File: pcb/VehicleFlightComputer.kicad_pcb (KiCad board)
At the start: 4 copper layers, 50 x 50 mm, 65 parts, among them J1 FFC2B28-24-G, J3 USB_C_Receptacle, J4 Debug, Q1 S8050, SW1 B3U-1000P, SW2 B3U-1000P, U1 STM32H533VET6, U2 LIS2MDL, U3 LSM6DSV32X, U4 MCP2221A-I/ST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

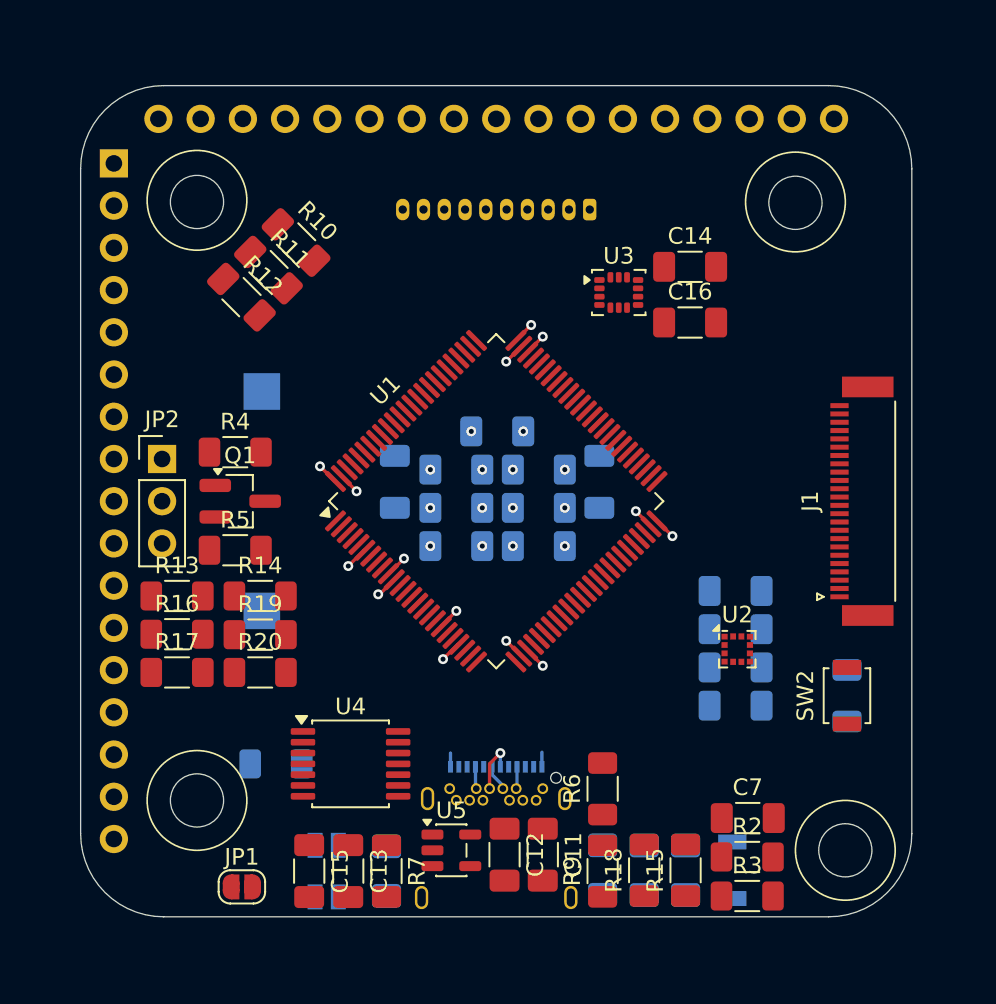
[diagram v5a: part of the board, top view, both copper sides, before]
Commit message: Updated vehicle stack-up edge-cuts for `VehicleMiscellaneousBoard` and `VehicleFlightComputer`.
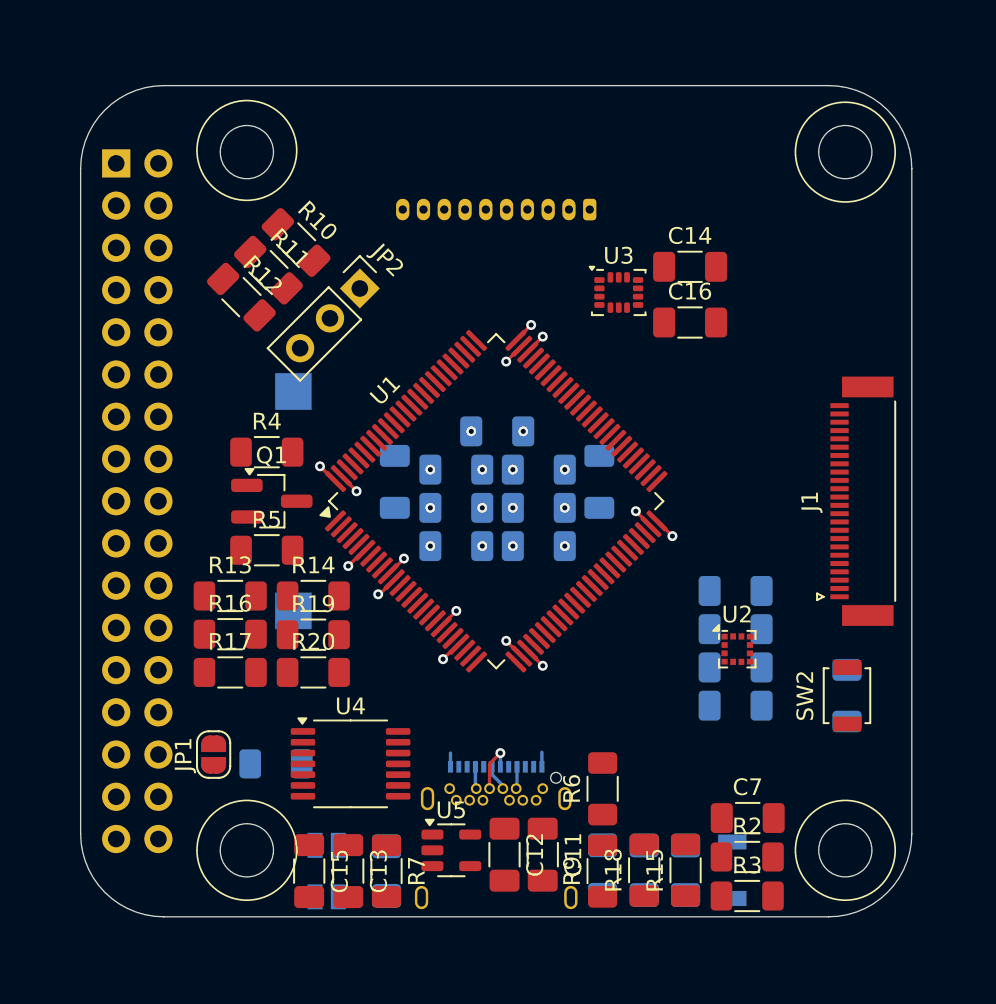
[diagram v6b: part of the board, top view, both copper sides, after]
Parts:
- removed H1, H3: MountingHole, MountingHole:MountingHole_3.2mm_M3
- moved JP2 15.7 mm to (141.8, 87.2), turned to -45 degrees
- moved JP1 8.14 mm to (133.0, 115.2), turned to 90 degrees
- moved H2 4.24 mm to (135.0, 79.0)
- moved H4 4.24 mm to (135.0, 121.0)
- moved R13 3.20 mm to (134.0, 105.7)
- moved R14 3.20 mm to (139.0, 105.7)
- moved R16 3.20 mm to (134.0, 108.0)
- moved R17 3.20 mm to (134.0, 110.3)
- moved R19 3.20 mm to (139.0, 108.0)
- moved R20 3.20 mm to (139.0, 110.3)
- moved BZ1 1.90 mm to (137.8, 100.0)
- moved Q1 1.90 mm to (136.5, 100.0)
- moved R4 1.90 mm to (136.2, 97.0)
- moved R5 1.90 mm to (136.2, 103.0)

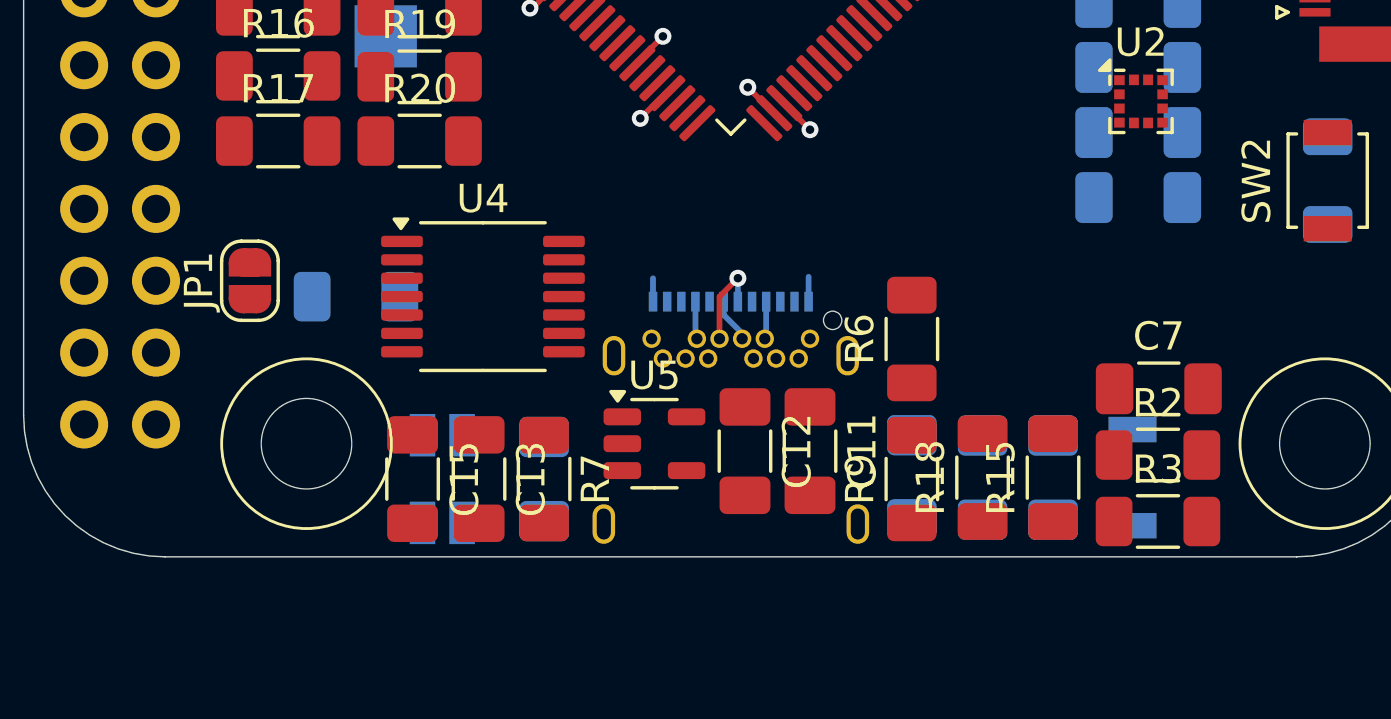
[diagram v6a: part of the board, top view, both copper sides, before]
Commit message: Placed footprints and routed USB-UART bridge and reset mechanism for `VehicleFlightComputer`.
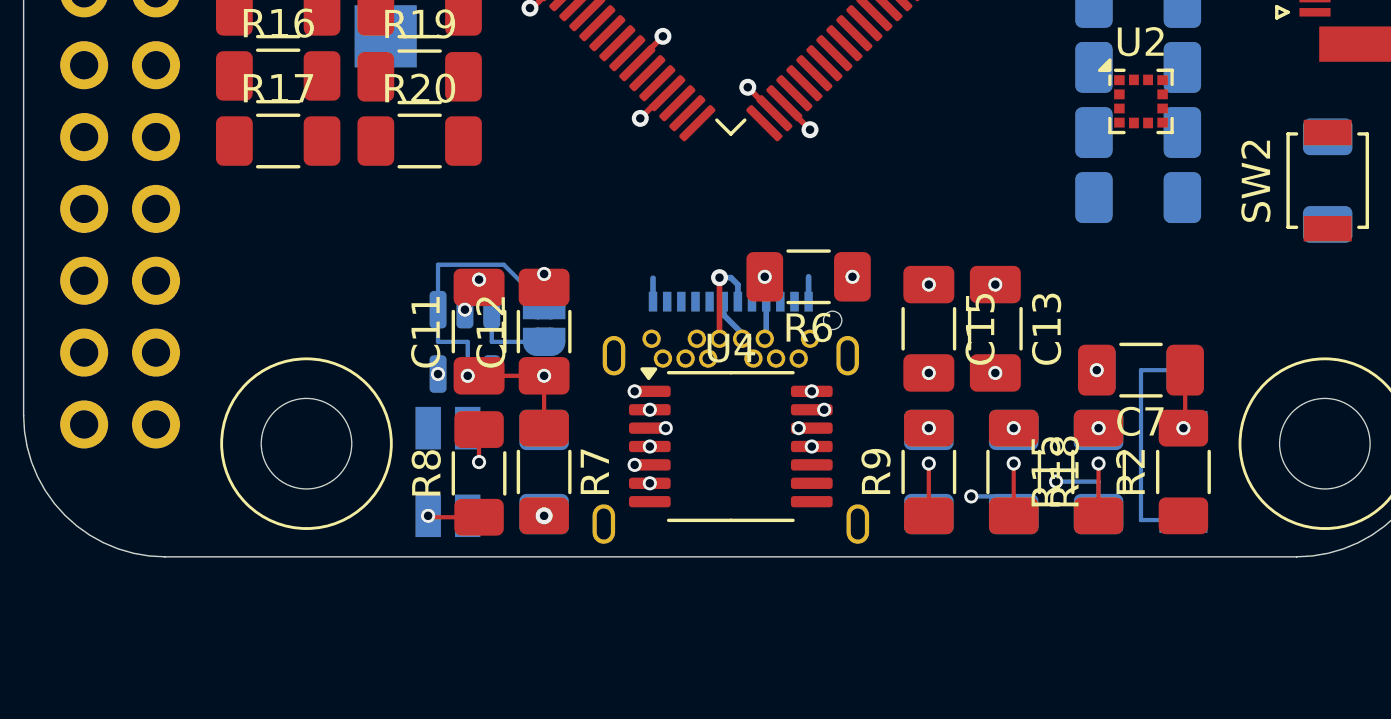
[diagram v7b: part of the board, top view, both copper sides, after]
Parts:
- JP1, R3, U5: moved to B.Cu
- R8: moved to F.Cu
- moved C13 19.0 mm to (159.3, 116.9)
- moved C15 19.0 mm to (157.0, 116.9)
- moved C11 12.4 mm to (141.1, 117.0), turned to 90 degrees
- moved JP1 10.5 mm to (143.4, 116.7), turned to -90 degrees
- moved U4 10.2 mm to (150.0, 121.1)
- moved C12 8.26 mm to (143.4, 117.0), turned to 90 degrees
- moved R8 7.61 mm to (141.1, 122.1), turned to 90 degrees
- moved U5 7.61 mm to (140.6, 117.4), turned to -90 degrees
- moved R3 5.38 mm to (164.5, 118.4), turned to 180 degrees
- moved R6 4.26 mm to (152.8, 115.1), turned to 180 degrees
- moved SW1 1.81 mm to (166.0, 122.0), turned to -90 degrees
- moved D3 1.62 mm to (163.0, 122.0)
- moved R15 1.62 mm to (163.0, 122.0)
- moved D4 1.12 mm to (160.0, 122.0)
- moved R18 1.12 mm to (160.0, 122.0), turned to -90 degrees
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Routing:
- net Net-(JP1-A): track 2.66 -> 24.6 mm, vias 0 -> 2
- net Net-(D3-K): track 0.00 -> 19.6 mm, vias 0 -> 2
- net serial_reset: track 0.00 -> 18.1 mm, vias 0 -> 2
- net Net-(D4-K): track 0.00 -> 15.3 mm, vias 0 -> 2
- net serial_rx: track 0.00 -> 13.8 mm, vias 0 -> 1
- net serial_tx: track 0.00 -> 11.6 mm, vias 0 -> 1
- net RESET: track 0.00 -> 8.73 mm, vias 0 -> 1
- net Net-(R3-Pad1): track 0.00 -> 8.35 mm
- net +3.3V: track 10.6 -> 18.0 mm, vias 15 -> 24
- net Net-(U4-D-): track 3.24 -> 9.36 mm, vias 1 -> 2
- net Net-(U4-D+): track 1.58 -> 7.27 mm, vias 0 -> 1
- net Net-(JP1-B): track 0.00 -> 2.99 mm
- net Net-(J3-CC1): track 0.00 -> 1.07 mm, vias 0 -> 1
- net Net-(D4-A): vias 0 -> 1
- net Net-(D3-A): vias 0 -> 1
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
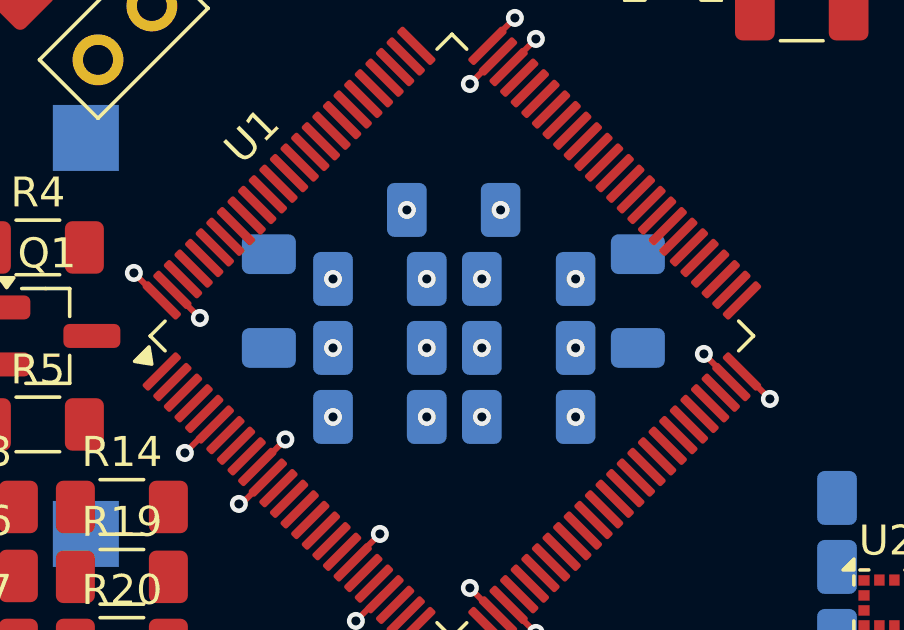
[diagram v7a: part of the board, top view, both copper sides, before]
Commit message: Routed VCAP.
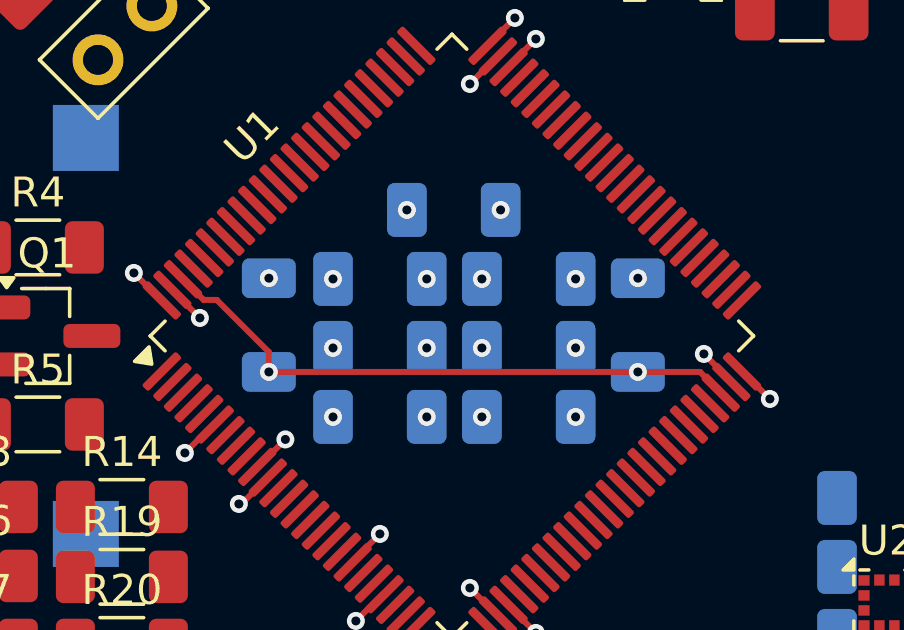
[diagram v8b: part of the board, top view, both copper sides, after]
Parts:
- moved C10 0.80 mm to (143.9, 99.6)
- moved C9 0.80 mm to (156.2, 99.6)
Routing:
- net VCAP: track 0.00 -> 19.9 mm, vias 0 -> 2
- net GND: vias 21 -> 23
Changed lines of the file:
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@@
 	(footprint "Capacitor_SMD:C_1206_3216Metric_Pad1.33x1.80mm_HandSolder"
 		(layer "B.Cu")
-		(at 156.2 98.8375 90)
+		(at 156.2 99.6375 90)
 		(descr "Capacitor SMD 1206 (3216 Metric), square (rectangular) end terminal, IPC-7351 nominal with elongated pad for handsoldering. (Body size source: IPC-SM-782 page 76, https://www.pcb-3d.com/wordpress/wp-content/uploads/ipc-sm-782a_amendment_1_and_2.pdf), generated with kicad-footprint-generator")
 		(tags "capacitor handsolder")
@@
 	(footprint "Capacitor_SMD:C_1206_3216Metric_Pad1.33x1.80mm_HandSolder"
 		(layer "B.Cu")
-		(at 143.9 98.8375 90)
+		(at 143.9 99.6375 90)
 		(descr "Capacitor SMD 1206 (3216 Metric), square (rectangular) end terminal, IPC-7351 nominal with elongated pad for handsoldering. (Body size source: IPC-SM-782 page 76, https://www.pcb-3d.com/wordpress/wp-content/uploads/ipc-sm-782a_amendment_1_and_2.pdf), generated with kicad-footprint-generator")
 		(tags "capacitor handsolder")
@@
 	)
 	(via
+		(at 143.9 98.075)
+		(size 0.6)
+		(drill 0.3)
+		(layers "F.Cu" "B.Cu")
+		(net 4)
+	)
+	(via
 		(at 162.9375 118.4)
 		(size 0.5)
@@
 	)
 	(via
+		(at 156.2 98.075)
+		(size 0.6)
+		(drill 0.3)
+		(layers "F.Cu" "B.Cu")
+		(net 4)
+	)
+	(via
 		(at 154.125002 98.100001)
 		(size 0.6)
@@
 	)
 	(segment
+		(start 143.9 101.2)
+		(end 143.9 100.5375)
+		(width 0.2)
+		(layer "F.Cu")
+		(net 39)
+	)
+	(segment
+		(start 143.9 100.5375)
+		(end 142.1615 98.799)
+		(width 0.2)
+		(layer "F.Cu")
+		(net 39)
+	)
+	(segment
+		(start 156.2 101.2)
+		(end 158.271067 101.2)
+		(width 0.2)
+		(layer "F.Cu")
+		(net 39)
+	)
+	(segment
+		(start 158.271067 101.2)
+		(end 158.962578 101.891511)
+		(width 0.2)
+		(layer "F.Cu")
+		(net 39)
+	)
+	(segment
+		(start 143.9 101.2)
+		(end 156.2 101.2)
+		(width 0.2)
+		(layer "F.Cu")
+		(net 39)
+	)
+	(segment
+		(start 141.727933 98.799)
+		(end 141.037422 98.108489)
+		(width 0.2)
+		(layer "F.Cu")
+		(net 39)
+	)
+	(segment
+		(start 142.1615 98.799)
+		(end 141.727933 98.799)
+		(width 0.2)
+		(layer "F.Cu")
+		(net 39)
+	)
+	(via
+		(at 156.2 101.2)
+		(size 0.6)
+		(drill 0.3)
+		(layers "F.Cu" "B.Cu")
+		(net 39)
+	)
+	(via
+		(at 143.9 101.2)
+		(size 0.6)
+		(drill 0.3)
+		(layers "F.Cu" "B.Cu")
+		(net 39)
+	)
+	(segment
